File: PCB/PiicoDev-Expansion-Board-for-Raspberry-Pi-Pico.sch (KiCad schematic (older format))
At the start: 23 parts, among them J1 PiicoDev, J2 JST PH, J3 , J4 , Q1 DMG3415U-7, U1 MCP73832-2-OT

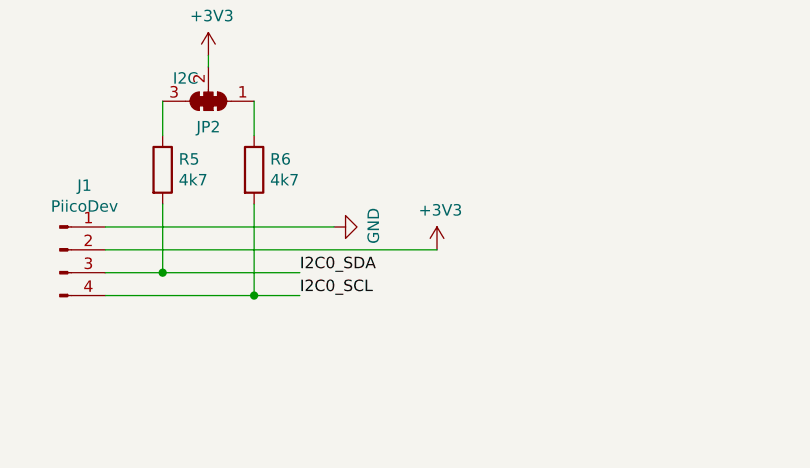
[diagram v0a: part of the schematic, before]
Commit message: Add 120R to SCL & SDA. Improve silk screen.
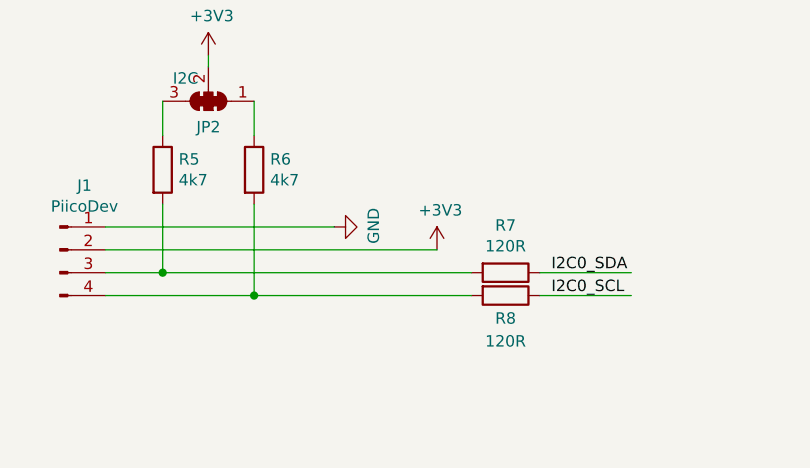
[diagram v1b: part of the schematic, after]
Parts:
- added R7, R8: 120R, Resistor_SMD:R_0402_1005Metric, symbol Device:R
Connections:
- net I2C0_SCL: now also R8.1; no longer J1.4 (Pin_4), R6.2
- net I2C0_SDA: now also R7.1; no longer J1.3 (Pin_3), R5.2
- new net: J1.3 (Pin_3), R5.2, R7.2
- new net: J1.4 (Pin_4), R6.2, R8.2
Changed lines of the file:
@@
 Sheet 1 1
 Title "Expansion Board for Raspberry Pi Pico"
-Date "2021-03-23"
-Rev "v10"
+Date "2021-10-29"
+Rev "v11"
 Comp "Core Electronics"
 Comment1 "Michael Ruppe"
@@
 $EndComp
 $Comp
-L power:VBUS #PWR?
+L power:VBUS #PWR05
 U 1 1 5FF3CDFC
 P 2300 3700
-F 0 "#PWR?" H 2300 3550 50  0001 C CNN
+F 0 "#PWR05" H 2300 3550 50  0001 C CNN
 F 1 "VBUS" H 2315 3873 50  0000 C CNN
 F 2 "" H 2300 3700 50  0001 C CNN
@@
 	2300 3950 2300 3850
 $Comp
-L power:GND #PWR?
+L power:GND #PWR06
 U 1 1 5FF3D73B
 P 2300 4950
-F 0 "#PWR?" H 2300 4700 50  0001 C CNN
+F 0 "#PWR06" H 2300 4700 50  0001 C CNN
 F 1 "GND" H 2305 4777 50  0000 C CNN
 F 2 "" H 2300 4950 50  0001 C CNN
@@
 	2300 4950 2300 4650
 $Comp
-L CoreElectronics_Power-Symbols:VBAT #PWR?
+L CoreElectronics_Power-Symbols:VBAT #PWR010
 U 1 1 5FF3DA40
 P 3300 3700
-F 0 "#PWR?" H 3300 3550 50  0001 C CNN
+F 0 "#PWR010" H 3300 3550 50  0001 C CNN
 F 1 "VBAT" H 3315 3873 50  0000 C CNN
 F 2 "" H 3300 3700 50  0001 C CNN
@@
 Connection ~ 3300 4150
 $Comp
-L power:GND #PWR?
+L power:GND #PWR011
 U 1 1 5FF3DFDD
 P 3300 4550
-F 0 "#PWR?" H 3300 4300 50  0001 C CNN
+F 0 "#PWR011" H 3300 4300 50  0001 C CNN
 F 1 "GND" H 3305 4377 50  0000 C CNN
 F 2 "" H 3300 4550 50  0001 C CNN
@@
 	2800 4750 2800 4650
 $Comp
-L power:VBUS #PWR?
+L power:VBUS #PWR08
 U 1 1 5FF3EBC7
 P 2800 5050
-F 0 "#PWR?" H 2800 4900 50  0001 C CNN
+F 0 "#PWR08" H 2800 4900 50  0001 C CNN
 F 1 "VBUS" H 2815 5223 50  0000 C CNN
 F 2 "" H 2800 5050 50  0001 C CNN
@@
 	2300 4650 2300 4550
 $Comp
-L power:VBUS #PWR?
+L power:VBUS #PWR03
 U 1 1 5FF40002
 P 1600 2000
-F 0 "#PWR?" H 1600 1850 50  0001 C CNN
+F 0 "#PWR03" H 1600 1850 50  0001 C CNN
 F 1 "VBUS" H 1615 2173 50  0000 C CNN
 F 2 "" H 1600 2000 50  0001 C CNN
@@
 	2000 2000 2000 1800
 $Comp
-L CoreElectronics_Power-Symbols:VBAT #PWR?
+L CoreElectronics_Power-Symbols:VBAT #PWR02
 U 1 1 5FF42981
 P 1600 1350
-F 0 "#PWR?" H 1600 1200 50  0001 C CNN
+F 0 "#PWR02" H 1600 1200 50  0001 C CNN
 F 1 "VBAT" H 1615 1523 50  0000 C CNN
 F 2 "" H 1600 1350 50  0001 C CNN
@@
 $EndComp
 $Comp
-L power:VBUS #PWR?
+L power:VBUS #PWR016
 U 1 1 5FF4CA1E
 P 8600 1800
-F 0 "#PWR?" H 8600 1650 50  0001 C CNN
+F 0 "#PWR016" H 8600 1650 50  0001 C CNN
 F 1 "VBUS" H 8615 1973 50  0000 C CNN
 F 2 "" H 8600 1800 50  0001 C CNN
@@
 	3650 1550 3800 1550
 $Comp
-L power:GND #PWR?
+L power:GND #PWR014
 U 1 1 5FF8B384
 P 3800 1650
-F 0 "#PWR?" H 3800 1400 50  0001 C CNN
+F 0 "#PWR014" H 3800 1400 50  0001 C CNN
 F 1 "GND" H 3805 1477 50  0000 C CNN
 F 2 "" H 3800 1650 50  0001 C CNN
@@
 $EndComp
 $Comp
-L power:+3V3 #PWR?
+L power:+3V3 #PWR017
 U 1 1 5FF54388
 P 8800 1400
-F 0 "#PWR?" H 8800 1250 50  0001 C CNN
+F 0 "#PWR017" H 8800 1250 50  0001 C CNN
 F 1 "+3V3" H 8815 1573 50  0000 C CNN
 F 2 "" H 8800 1400 50  0001 C CNN
@@
 	8800 2200 9350 2200
 $Comp
-L power:+3V3 #PWR?
+L power:+3V3 #PWR012
 U 1 1 5FF568F1
 P 3650 6800
-F 0 "#PWR?" H 3650 6650 50  0001 C CNN
+F 0 "#PWR012" H 3650 6650 50  0001 C CNN
 F 1 "+3V3" H 3665 6973 50  0000 C CNN
 F 2 "" H 3650 6800 50  0001 C CNN
@@
 	1    0    0    -1
 $EndComp
-Text Label 3050 6900 0    50   ~ 0
+Text Label 4150 6900 0    50   ~ 0
 I2C0_SDA
-Text Label 3050 7000 0    50   ~ 0
+Text Label 4150 7000 0    50   ~ 0
 I2C0_SCL
-Wire Wire Line
-	3050 7000 2850 7000
 Wire Wire Line
 	2200 6900 2450 6900
@@
 $EndComp
 $Comp
-L CoreElectronics_Power-Symbols:VBAT #PWR?
+L CoreElectronics_Power-Symbols:VBAT #PWR013
 U 1 1 5FF89B75
 P 3800 1550
-F 0 "#PWR?" H 3800 1400 50  0001 C CNN
+F 0 "#PWR013" H 3800 1400 50  0001 C CNN
 F 1 "VBAT" H 3815 1723 50  0000 C CNN
 F 2 "" H 3800 1550 50  0001 C CNN
@@
 	2300 3850 2300 3700
 $Comp
-L power:GND #PWR?
+L power:GND #PWR01
 U 1 1 600A0AD3
 P 1000 4200
-F 0 "#PWR?" H 1000 3950 50  0001 C CNN
+F 0 "#PWR01" H 1000 3950 50  0001 C CNN
 F 1 "GND" H 1005 4027 50  0000 C CNN
 F 2 "" H 1000 4200 50  0001 C CNN
@@
 	1700 4350 1750 4350
 $Comp
-L power:GND #PWR?
+L power:GND #PWR018
 U 1 1 600B5B14
 P 9250 3950
-F 0 "#PWR?" H 9250 3700 50  0001 C CNN
+F 0 "#PWR018" H 9250 3700 50  0001 C CNN
 F 1 "GND" H 9255 3777 50  0000 C CNN
 F 2 "" H 9250 3950 50  0001 C CNN
@@
 	9250 3500 9250 3950
 $Comp
-L power:GND #PWR?
+L power:GND #PWR015
 U 1 1 600C2F3C
 P 6550 3950
-F 0 "#PWR?" H 6550 3700 50  0001 C CNN
+F 0 "#PWR015" H 6550 3700 50  0001 C CNN
 F 1 "GND" H 6555 3777 50  0000 C CNN
 F 2 "" H 6550 3950 50  0001 C CNN
@@
 	6550 2000 7050 2000
 $Comp
-L power:GND #PWR?
+L power:GND #PWR09
 U 1 1 6024DB1A
 P 3200 6700
-F 0 "#PWR?" H 3200 6450 50  0001 C CNN
+F 0 "#PWR09" H 3200 6450 50  0001 C CNN
 F 1 "GND" H 3205 6527 50  0000 C CNN
 F 2 "" H 3200 6700 50  0001 C CNN
@@
 Connection ~ 2000 2000
 $Comp
-L power:GND #PWR?
+L power:GND #PWR04
 U 1 1 603E8A9C
 P 2000 2350
-F 0 "#PWR?" H 2000 2100 50  0001 C CNN
+F 0 "#PWR04" H 2000 2100 50  0001 C CNN
 F 1 "GND" H 2005 2177 50  0000 C CNN
 F 2 "" H 2000 2350 50  0001 C CNN
@@
 Connection ~ 2450 6900
 Wire Wire Line
-	2450 6900 3050 6900
-Wire Wire Line
 	2850 6600 2850 7000
 Connection ~ 2850 7000
@@
 	2850 7000 2200 7000
 $Comp
-L power:+3V3 #PWR?
+L power:+3V3 #PWR07
 U 1 1 60429F8E
 P 2650 5950
-F 0 "#PWR?" H 2650 5800 50  0001 C CNN
+F 0 "#PWR07" H 2650 5800 50  0001 C CNN
 F 1 "+3V3" H 2665 6123 50  0000 C CNN
 F 2 "" H 2650 5950 50  0001 C CNN
@@
 Wire Wire Line
 	2650 5950 2650 6000
+$Comp
+L Device:R R7
+U 1 1 617CD86B
+P 3950 6900
+F 0 "R7" V 3743 6900 50  0000 C CNN
+F 1 "120R" V 3834 6900 50  0000 C CNN
+F 2 "Resistor_SMD:R_0402_1005Metric" V 3880 6900 50  0001 C CNN
+F 3 "~" H 3950 6900 50  0001 C CNN
+	1    3950 6900
+	0    1    1    0
+$EndComp
+$Comp
+L Device:R R8
+U 1 1 617CE6D1
+P 3950 7000
+F 0 "R8" V 4050 7000 50  0000 C CNN
+F 1 "120R" V 4150 7000 50  0000 C CNN
+F 2 "Resistor_SMD:R_0402_1005Metric" V 3880 7000 50  0001 C CNN
+F 3 "~" H 3950 7000 50  0001 C CNN
+	1    3950 7000
+	0    1    1    0
+$EndComp
+Wire Wire Line
+	2450 6900 3800 6900
+Wire Wire Line
+	2850 7000 3800 7000
+Wire Wire Line
+	4100 6900 4500 6900
+Wire Wire Line
+	4100 7000 4500 7000
 $EndSCHEMATC

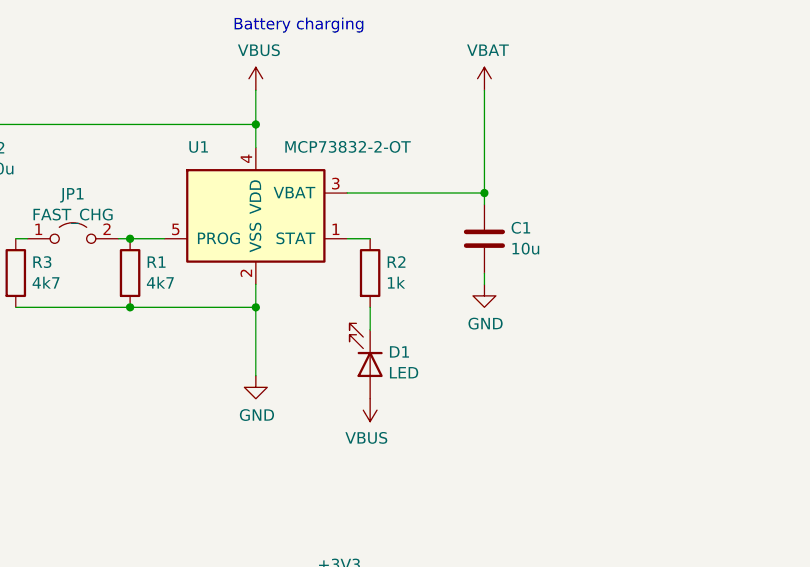
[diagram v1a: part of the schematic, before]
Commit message: Change LED Resistor from 1k to 4.7k
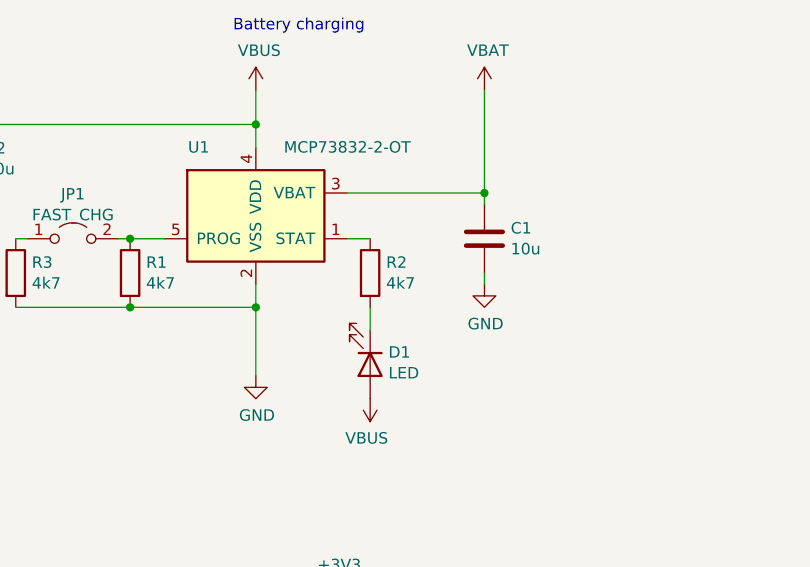
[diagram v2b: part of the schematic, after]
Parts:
- R2: value 1k -> 4k7
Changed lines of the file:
@@
 P 2800 4500
 F 0 "R2" H 2870 4546 50  0000 L CNN
-F 1 "1k" H 2870 4455 50  0000 L CNN
+F 1 "4k7" H 2870 4455 50  0000 L CNN
 F 2 "Resistor_SMD:R_0402_1005Metric" V 2730 4500 50  0001 C CNN
 F 3 "~" H 2800 4500 50  0001 C CNN

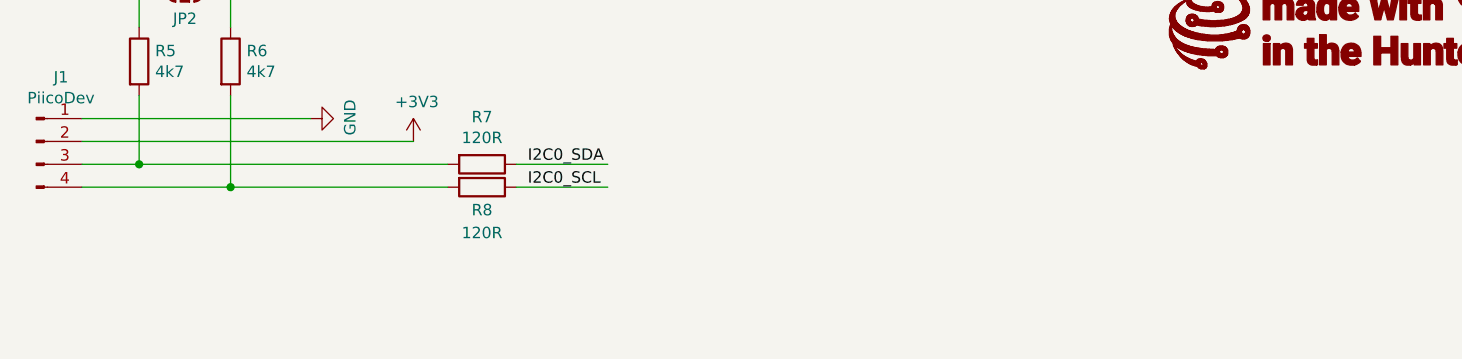
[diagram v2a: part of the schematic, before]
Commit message: Update schematic pdf to v11
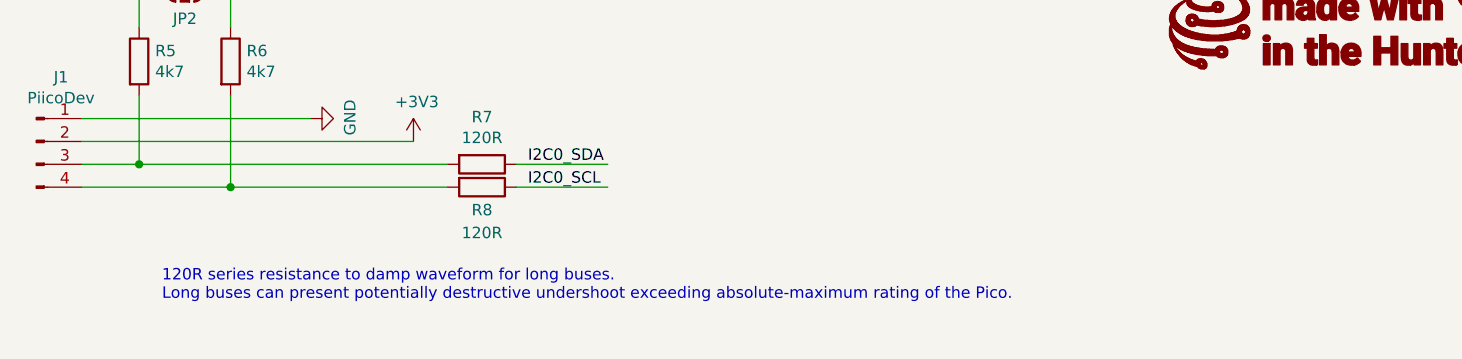
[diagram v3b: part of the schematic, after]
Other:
- note added: "120R series resistance to damp waveform for long buses.\nLong buses can present potentially destructive undershoot exceeding absolute-maximum rating of the Pico."
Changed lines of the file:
@@
 $EndComp
 $Comp
-L power:VBUS #PWR05
+L power:VBUS #PWR?
 U 1 1 5FF3CDFC
 P 2300 3700
-F 0 "#PWR05" H 2300 3550 50  0001 C CNN
+F 0 "#PWR?" H 2300 3550 50  0001 C CNN
 F 1 "VBUS" H 2315 3873 50  0000 C CNN
 F 2 "" H 2300 3700 50  0001 C CNN
@@
 	2300 3950 2300 3850
 $Comp
-L power:GND #PWR06
+L power:GND #PWR?
 U 1 1 5FF3D73B
 P 2300 4950
-F 0 "#PWR06" H 2300 4700 50  0001 C CNN
+F 0 "#PWR?" H 2300 4700 50  0001 C CNN
 F 1 "GND" H 2305 4777 50  0000 C CNN
 F 2 "" H 2300 4950 50  0001 C CNN
@@
 	2300 4950 2300 4650
 $Comp
-L CoreElectronics_Power-Symbols:VBAT #PWR010
+L CoreElectronics_Power-Symbols:VBAT #PWR?
 U 1 1 5FF3DA40
 P 3300 3700
-F 0 "#PWR010" H 3300 3550 50  0001 C CNN
+F 0 "#PWR?" H 3300 3550 50  0001 C CNN
 F 1 "VBAT" H 3315 3873 50  0000 C CNN
 F 2 "" H 3300 3700 50  0001 C CNN
@@
 Connection ~ 3300 4150
 $Comp
-L power:GND #PWR011
+L power:GND #PWR?
 U 1 1 5FF3DFDD
 P 3300 4550
-F 0 "#PWR011" H 3300 4300 50  0001 C CNN
+F 0 "#PWR?" H 3300 4300 50  0001 C CNN
 F 1 "GND" H 3305 4377 50  0000 C CNN
 F 2 "" H 3300 4550 50  0001 C CNN
@@
 	2800 4750 2800 4650
 $Comp
-L power:VBUS #PWR08
+L power:VBUS #PWR?
 U 1 1 5FF3EBC7
 P 2800 5050
-F 0 "#PWR08" H 2800 4900 50  0001 C CNN
+F 0 "#PWR?" H 2800 4900 50  0001 C CNN
 F 1 "VBUS" H 2815 5223 50  0000 C CNN
 F 2 "" H 2800 5050 50  0001 C CNN
@@
 	2300 4650 2300 4550
 $Comp
-L power:VBUS #PWR03
+L power:VBUS #PWR?
 U 1 1 5FF40002
 P 1600 2000
-F 0 "#PWR03" H 1600 1850 50  0001 C CNN
+F 0 "#PWR?" H 1600 1850 50  0001 C CNN
 F 1 "VBUS" H 1615 2173 50  0000 C CNN
 F 2 "" H 1600 2000 50  0001 C CNN
@@
 	2000 2000 2000 1800
 $Comp
-L CoreElectronics_Power-Symbols:VBAT #PWR02
+L CoreElectronics_Power-Symbols:VBAT #PWR?
 U 1 1 5FF42981
 P 1600 1350
-F 0 "#PWR02" H 1600 1200 50  0001 C CNN
+F 0 "#PWR?" H 1600 1200 50  0001 C CNN
 F 1 "VBAT" H 1615 1523 50  0000 C CNN
 F 2 "" H 1600 1350 50  0001 C CNN
@@
 $EndComp
 $Comp
-L power:VBUS #PWR016
+L power:VBUS #PWR?
 U 1 1 5FF4CA1E
 P 8600 1800
-F 0 "#PWR016" H 8600 1650 50  0001 C CNN
+F 0 "#PWR?" H 8600 1650 50  0001 C CNN
 F 1 "VBUS" H 8615 1973 50  0000 C CNN
 F 2 "" H 8600 1800 50  0001 C CNN
@@
 	3650 1550 3800 1550
 $Comp
-L power:GND #PWR014
+L power:GND #PWR?
 U 1 1 5FF8B384
 P 3800 1650
-F 0 "#PWR014" H 3800 1400 50  0001 C CNN
+F 0 "#PWR?" H 3800 1400 50  0001 C CNN
 F 1 "GND" H 3805 1477 50  0000 C CNN
 F 2 "" H 3800 1650 50  0001 C CNN
@@
 $EndComp
 $Comp
-L power:+3V3 #PWR017
+L power:+3V3 #PWR?
 U 1 1 5FF54388
 P 8800 1400
-F 0 "#PWR017" H 8800 1250 50  0001 C CNN
+F 0 "#PWR?" H 8800 1250 50  0001 C CNN
 F 1 "+3V3" H 8815 1573 50  0000 C CNN
 F 2 "" H 8800 1400 50  0001 C CNN
@@
 	8800 2200 9350 2200
 $Comp
-L power:+3V3 #PWR012
+L power:+3V3 #PWR?
 U 1 1 5FF568F1
 P 3650 6800
-F 0 "#PWR012" H 3650 6650 50  0001 C CNN
+F 0 "#PWR?" H 3650 6650 50  0001 C CNN
 F 1 "+3V3" H 3665 6973 50  0000 C CNN
 F 2 "" H 3650 6800 50  0001 C CNN
@@
 $EndComp
 $Comp
-L CoreElectronics_Power-Symbols:VBAT #PWR013
+L CoreElectronics_Power-Symbols:VBAT #PWR?
 U 1 1 5FF89B75
 P 3800 1550
-F 0 "#PWR013" H 3800 1400 50  0001 C CNN
+F 0 "#PWR?" H 3800 1400 50  0001 C CNN
 F 1 "VBAT" H 3815 1723 50  0000 C CNN
 F 2 "" H 3800 1550 50  0001 C CNN
@@
 	2300 3850 2300 3700
 $Comp
-L power:GND #PWR01
+L power:GND #PWR?
 U 1 1 600A0AD3
 P 1000 4200
-F 0 "#PWR01" H 1000 3950 50  0001 C CNN
+F 0 "#PWR?" H 1000 3950 50  0001 C CNN
 F 1 "GND" H 1005 4027 50  0000 C CNN
 F 2 "" H 1000 4200 50  0001 C CNN
@@
 	1700 4350 1750 4350
 $Comp
-L power:GND #PWR018
+L power:GND #PWR?
 U 1 1 600B5B14
 P 9250 3950
-F 0 "#PWR018" H 9250 3700 50  0001 C CNN
+F 0 "#PWR?" H 9250 3700 50  0001 C CNN
 F 1 "GND" H 9255 3777 50  0000 C CNN
 F 2 "" H 9250 3950 50  0001 C CNN
@@
 	9250 3500 9250 3950
 $Comp
-L power:GND #PWR015
+L power:GND #PWR?
 U 1 1 600C2F3C
 P 6550 3950
-F 0 "#PWR015" H 6550 3700 50  0001 C CNN
+F 0 "#PWR?" H 6550 3700 50  0001 C CNN
 F 1 "GND" H 6555 3777 50  0000 C CNN
 F 2 "" H 6550 3950 50  0001 C CNN
@@
 	6550 2000 7050 2000
 $Comp
-L power:GND #PWR09
+L power:GND #PWR?
 U 1 1 6024DB1A
 P 3200 6700
-F 0 "#PWR09" H 3200 6450 50  0001 C CNN
+F 0 "#PWR?" H 3200 6450 50  0001 C CNN
 F 1 "GND" H 3205 6527 50  0000 C CNN
 F 2 "" H 3200 6700 50  0001 C CNN
@@
 Connection ~ 2000 2000
 $Comp
-L power:GND #PWR04
+L power:GND #PWR?
 U 1 1 603E8A9C
 P 2000 2350
-F 0 "#PWR04" H 2000 2100 50  0001 C CNN
+F 0 "#PWR?" H 2000 2100 50  0001 C CNN
 F 1 "GND" H 2005 2177 50  0000 C CNN
 F 2 "" H 2000 2350 50  0001 C CNN
@@
 	2850 7000 2200 7000
 $Comp
-L power:+3V3 #PWR07
+L power:+3V3 #PWR?
 U 1 1 60429F8E
 P 2650 5950
-F 0 "#PWR07" H 2650 5800 50  0001 C CNN
+F 0 "#PWR?" H 2650 5800 50  0001 C CNN
 F 1 "+3V3" H 2665 6123 50  0000 C CNN
 F 2 "" H 2650 5950 50  0001 C CNN
@@
 Wire Wire Line
 	4100 7000 4500 7000
+Text Notes 2550 7500 0    50   ~ 0
+120R series resistance to damp waveform for long buses.\nLong buses can present potentially destructive undershoot exceeding absolute-maximum rating of the Pico.
 $EndSCHEMATC
